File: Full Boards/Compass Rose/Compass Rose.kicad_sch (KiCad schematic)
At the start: 243 parts, among them J1 Program Header, Q10 2N3904, Q11 AO3401A, Q12 2N3904, Q7 AO3401A, Q8 2N3904, Q9 AO3401A, SW1 SW_MEC_5G, SW2 SW_MEC_5G, U1 ISO1044BD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

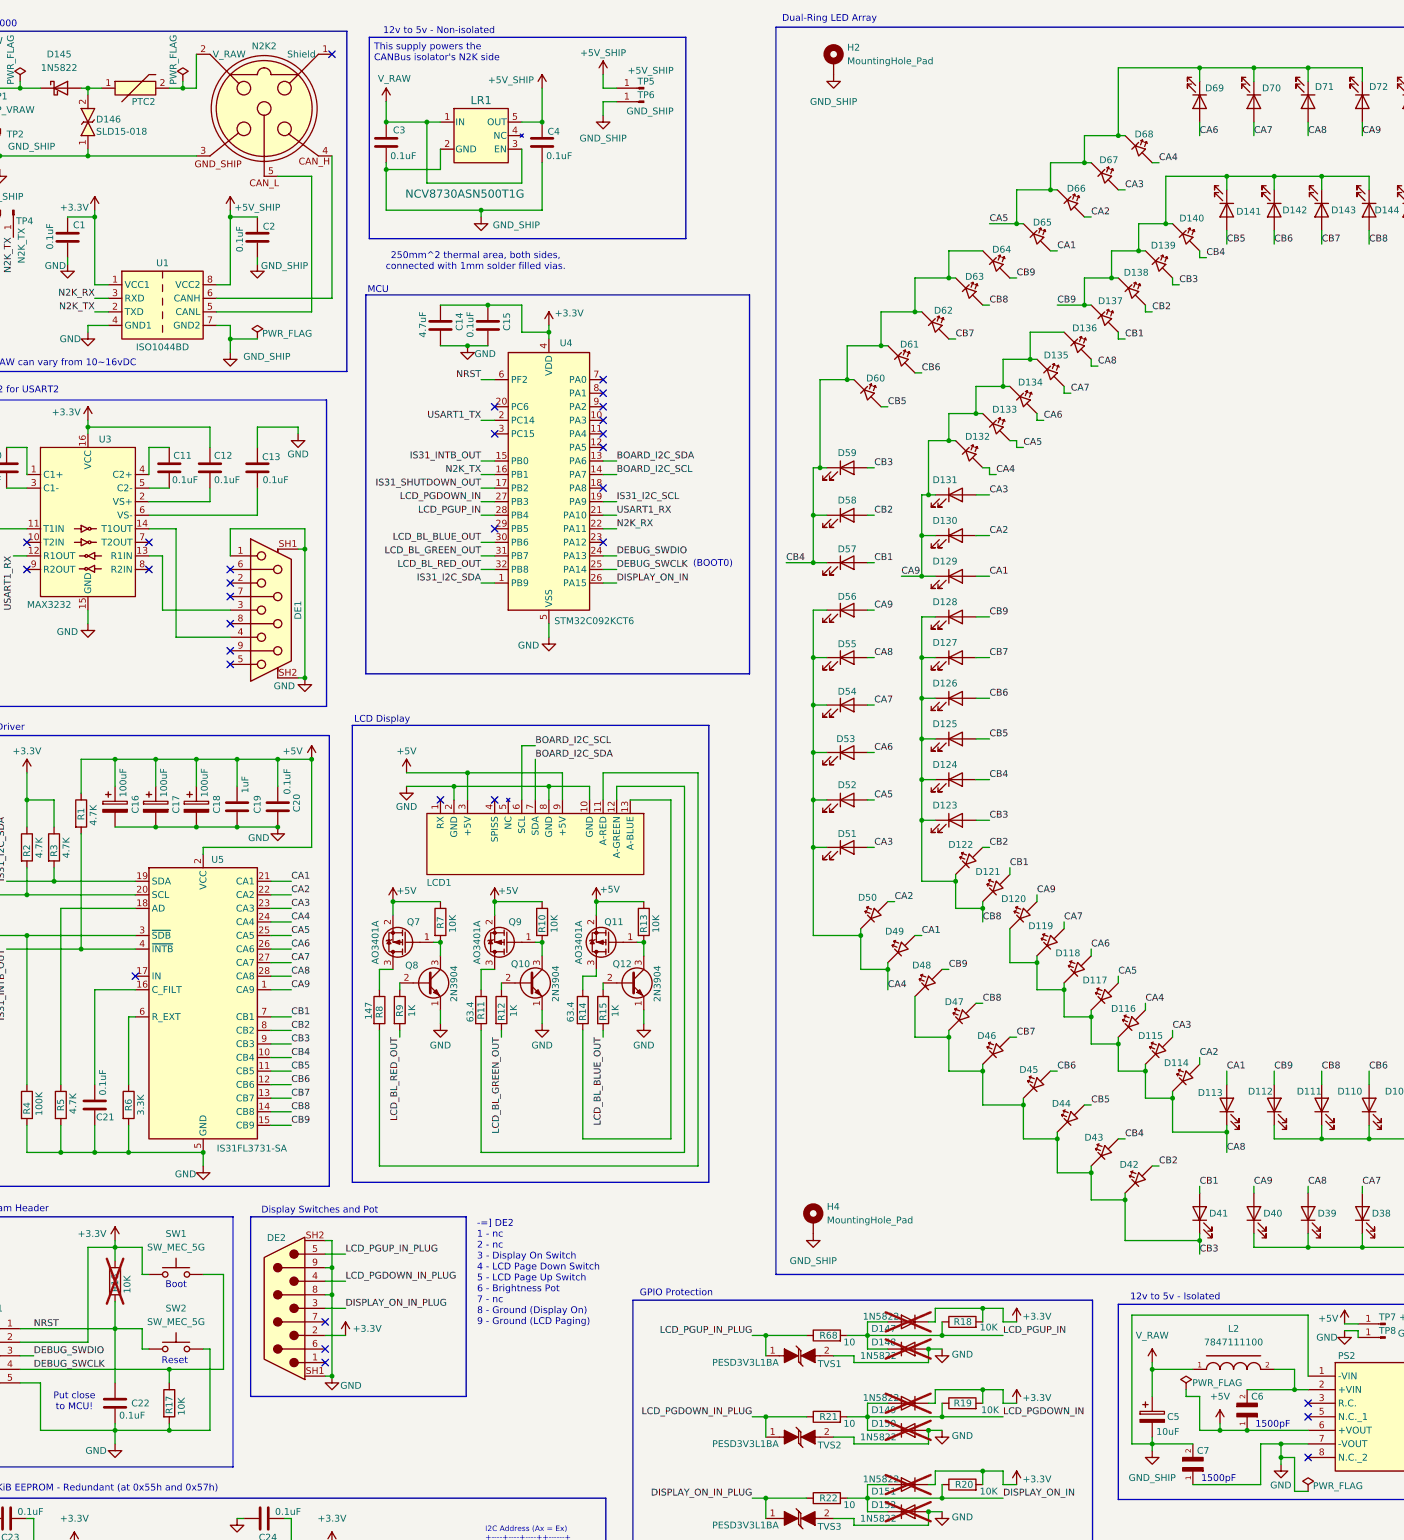
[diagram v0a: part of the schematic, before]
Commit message: Updated PCBs to swap RVS diodes from SLD15-018 to SLD22-018. Also swapped out the inductor from 7847111100 to PA4340.103NLT.
Signed-off-by: Madison Kelly <digital.mermaid@gmail.com>
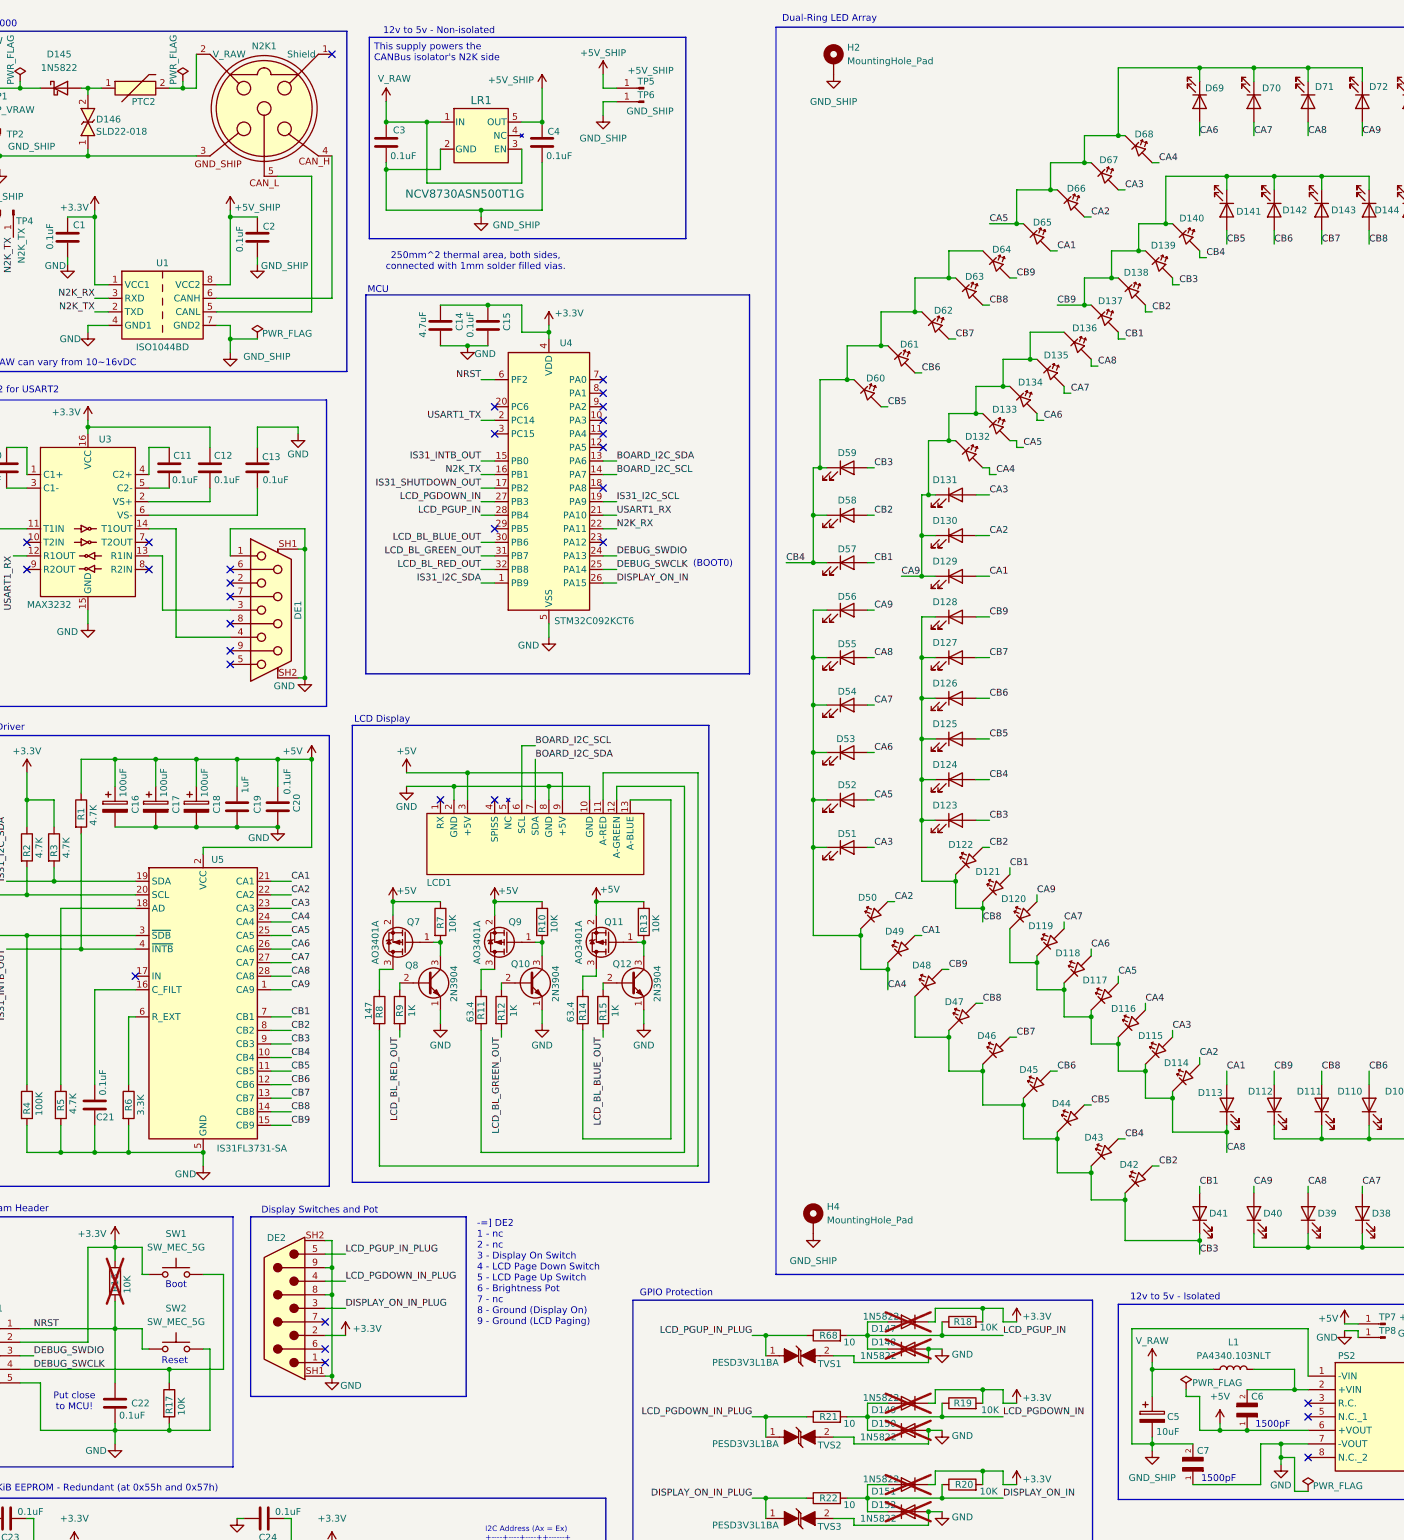
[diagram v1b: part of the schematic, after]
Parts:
- removed L2: 7847111100, mr-stuff:WE-RCIT_7847111100, symbol mr-parts:WE-RCIT
- added L1: PA4340.103NLT, mr-stuff:Pulse PA4340.103NLT, symbol Device:L
- D146: value SLD15-018 -> SLD22-018
- renumbered N2K2 to N2K1
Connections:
- net V_RAW: now also L1.1
- net at C6.2, PS2.2 (+VIN): now also L1.2
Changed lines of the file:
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@@
 	(wire
 		(pts
-			(xy 236.22 259.08) (xy 236.22 283.21)
+			(xy 236.22 261.62) (xy 236.22 283.21)
 		)
 		(stroke
@@
 	(wire
 		(pts
-			(xy 269.24 270.51) (xy 269.24 259.08)
+			(xy 269.24 270.51) (xy 269.24 261.62)
 		)
 		(stroke
@@
 	(wire
 		(pts
-			(xy 240.03 269.24) (xy 247.65 269.24)
+			(xy 240.03 269.24) (xy 251.46 269.24)
 		)
 		(stroke
@@
 	(wire
 		(pts
+			(xy 259.08 269.24) (xy 266.7 269.24)
+		)
+		(stroke
+			(width 0)
+			(type default)
+		)
+	)
+	(wire
+		(pts
 			(xy 279.4 234.95) (xy 279.4 236.22)
 		)
@@
 	(wire
 		(pts
-			(xy 266.7 269.24) (xy 262.89 269.24)
-		)
-		(stroke
-			(width 0)
-			(type default)
-		)
-	)
-	(wire
-		(pts
 			(xy 54.61 127) (xy 67.31 127)
 		)
@@
 	(wire
 		(pts
-			(xy 269.24 259.08) (xy 236.22 259.08)
+			(xy 269.24 261.62) (xy 236.22 261.62)
 		)
 		(stroke
@@
 	)
 	(symbol
+		(lib_id "Device:L")
+		(at 255.27 269.24 90)
+		(unit 1)
+		(exclude_from_sim no)
+		(in_bom yes)
+		(on_board yes)
+		(dnp no)
+		(fields_autoplaced yes)
+		(property "Reference" "L1"
+			(at 255.27 264.16 90)
+			(effects
+				(font
+					(size 1.27 1.27)
+				)
+			)
+		)
+		(property "Value" "PA4340.103NLT"
+			(at 255.27 266.7 90)
+			(effects
+				(font
+					(size 1.27 1.27)
+				)
+			)
+		)
+		(property "Footprint" "mr-stuff:Pulse PA4340.103NLT"
+			(at 255.27 269.24 0)
+			(effects
+				(font
+					(size 1.27 1.27)
+				)
+				(hide yes)
+			)
+		)
+		(property "Datasheet" "~"
+			(at 255.27 269.24 0)
+			(effects
+				(font
+					(size 1.27 1.27)
+				)
+				(hide yes)
+			)
+		)
+		(property "Description" "Inductor"
+			(at 255.27 269.24 0)
+			(effects
+				(font
+					(size 1.27 1.27)
+				)
+				(hide yes)
+			)
+		)
+		(pin "2"
+		)
+		(pin "1"
+		)
+		(instances
+			(project "Compass Rose"
+				(path "/e4671408-3e04-42c4-aa2c-7576ad4f645e"
+					(reference "L1")
+					(unit 1)
+				)
+			)
+		)
+	)
+	(symbol
 		(lib_id "Device:LED_45deg")
 		(at 374.65 196.85 0)
@@
 			)
 		)
-		(property "Value" "SLD15-018"
+		(property "Value" "SLD22-018"
 			(at 42.164 37.338 90)
 			(effects
@@
 		(on_board yes)
 		(dnp no)
-		(fields_autoplaced yes)
 		(property "Reference" "#PWR075"
 			(at 240.03 271.78 0)
@@
 		)
 		(property "Value" "V_RAW"
-			(at 240.03 262.89 0)
+			(at 240.03 263.906 0)
 			(effects
 				(font
@@
 		(on_board yes)
 		(dnp no)
-		(property "Reference" "N2K2"
+		(property "Reference" "N2K1"
 			(at 73.66 21.336 0)
 			(effects
@@
 			(project "Compass Rose"
 				(path "/e4671408-3e04-42c4-aa2c-7576ad4f645e"
-					(reference "N2K2")
+					(reference "N2K1")
 					(unit 1)
 				)
@@
 					(unit 1)
 				)
-			)
-		)
-	)
-	(symbol
-		(lib_id "mr-parts:WE-RCIT")
-		(at 255.27 269.24 0)
-		(unit 1)
-		(exclude_from_sim no)
-		(in_bom yes)
-		(on_board yes)
-		(dnp no)
-		(fields_autoplaced yes)
-		(property "Reference" "L2"
-			(at 255.27 261.62 0)
-			(effects
-				(font
-					(size 1.27 1.27)
-				)
-			)
-		)
-		(property "Value" "7847111100"
-			(at 255.27 264.16 0)
-			(effects
-				(font
-					(size 1.27 1.27)
-				)
-			)
-		)
-		(property "Footprint" "mr-stuff:WE-RCIT_7847111100"
-			(at 255.524 274.32 0)
-			(effects
-				(font
-					(size 1.27 1.27)
-				)
-				(justify bottom)
-				(hide yes)
-			)
-		)
-		(property "Datasheet" "https://www.we-online.com/components/products/datasheet/7847111100.pdf"
-			(at 255.27 269.24 0)
-			(effects
-				(font
-					(size 1.27 1.27)
-				)
-				(hide yes)
-			)
-		)
-		(property "Description" "10uH, 3A, rod-core inductor"
-			(at 255.27 269.24 0)
-			(effects
-				(font
-					(size 1.27 1.27)
-				)
-				(hide yes)
-			)
-		)
-		(pin "2"
-		)
-		(pin "1"
-		)
-		(instances
-			(project "Compass Rose"
-				(path "/e4671408-3e04-42c4-aa2c-7576ad4f645e"
-					(reference "L2")
-					(unit 1)
-				)
